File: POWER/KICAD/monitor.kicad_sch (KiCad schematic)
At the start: 3 parts, among them U5 INA228

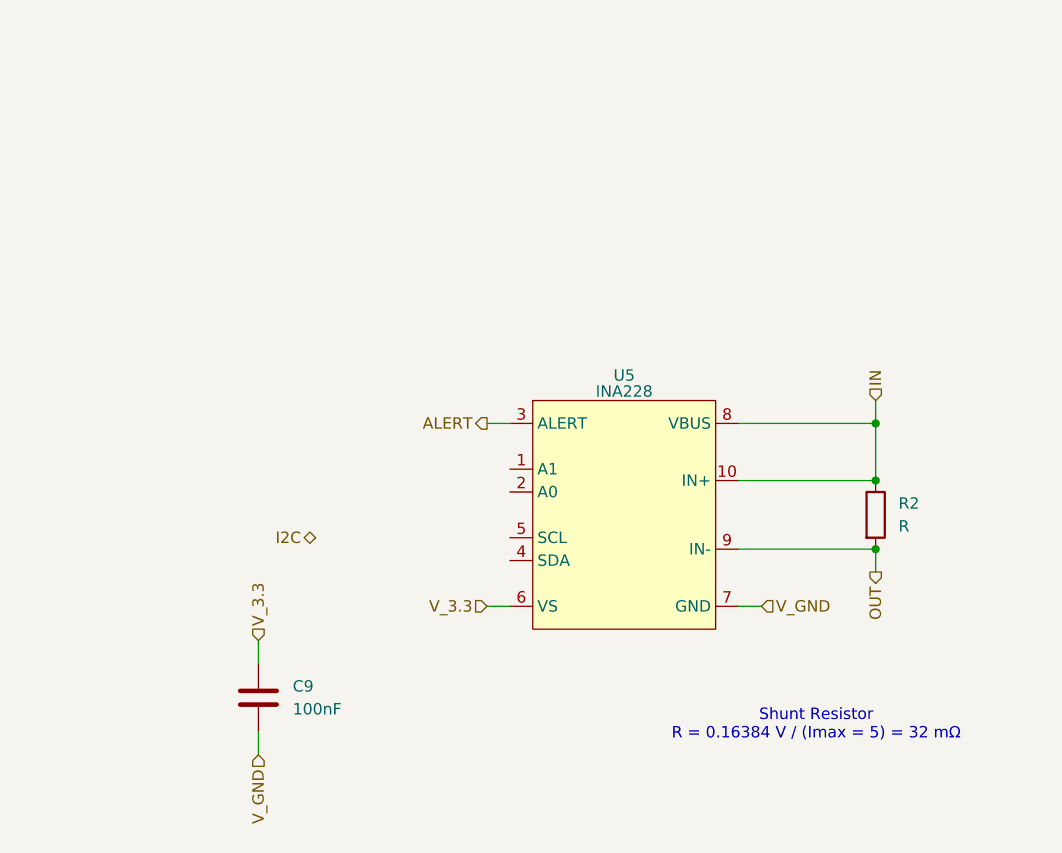
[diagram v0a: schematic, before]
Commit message: Updated Power Schematic / Kicad
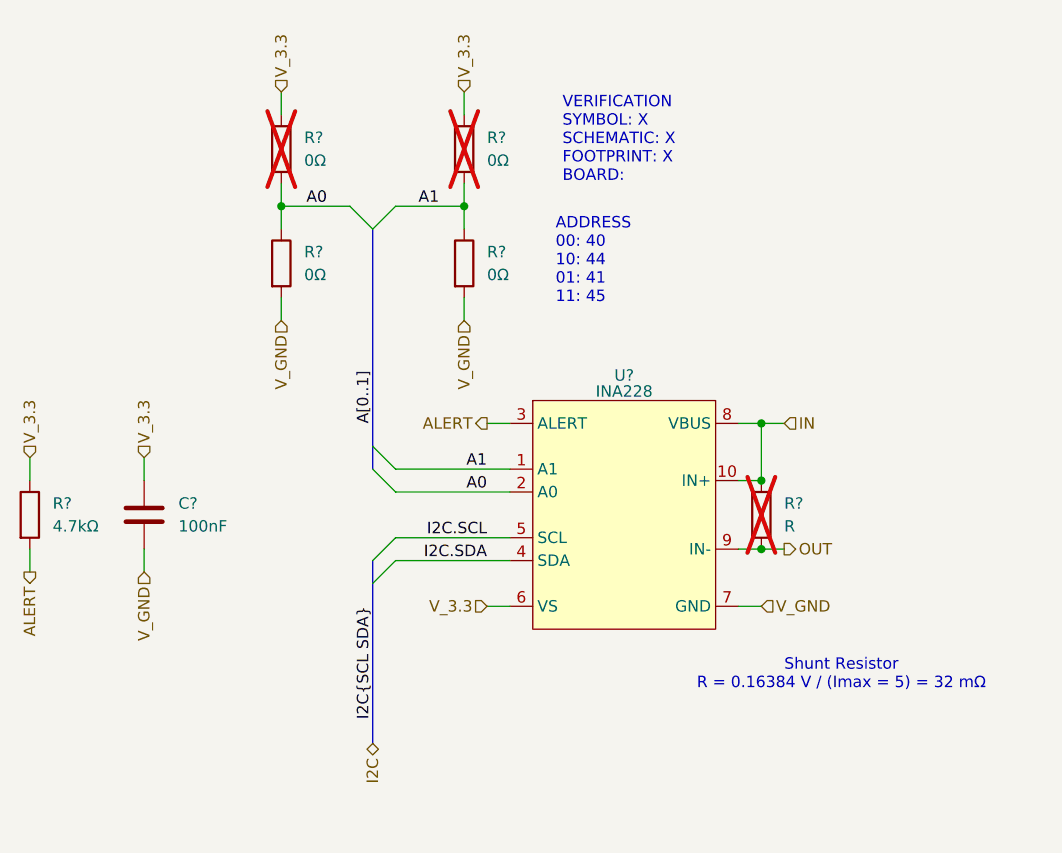
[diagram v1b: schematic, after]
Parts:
- removed R2: R, symbol Device:R
- added R? (x4): 0Ω, Resistor_SMD:R_0603_1608Metric, symbol Device:R
- added R?: 4.7kΩ, Resistor_SMD:R_0603_1608Metric, symbol Device:R
- added R?: R, symbol Device:R
- C?: renamed from C9; footprint (none) -> Capacitor_SMD:C_0603_1608Metric
- U?: renamed from U5; footprint (none) -> Package_SO:Texas_S-PDSO-G10_3x3mm_P0.5mm
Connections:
- net ALERT: now also R?.2
- net IN: now also R?.1
- net OUT: now also R?.2
- net V_3.3: now also R?.1, R?.1, R?.1
- net V_GND: now also R?.2, R?.2
- net A1: now reaches U?.1 (A1)
- net A1: now also R?.1, R?.2
- net A0: now reaches U?.2 (A0)
- net A0: now also R?.1, R?.2
- net I2C.SDA: now reaches U?.4 (SDA)
- net I2C.SCL: now reaches U?.5 (SCL)
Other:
- note added: "ADDRESS 00: 40 10: 44 01: 41 11: 45"
- note added: "VERIFICATION SYMBOL: X SCHEMATIC: X FOOTPRINT: X BOARD:"
- moved on the sheet: C?

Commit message: schematic design
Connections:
- net I2C.SCL renamed SCL
- net I2C.SDA renamed SDA
